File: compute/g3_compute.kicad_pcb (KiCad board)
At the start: 4 copper layers, 100 x 100 mm, 106 parts, among them IC101 CD74AC153M96, J101 Conn_01x09_Male, J102 53398-0871, J103 Temp_Connector_1x4, J104 53398-0671, J105 Conn_01x10_Male, J106 Pi_Connector, J107 Conn_01x06_Male, J108 CONSMA001-SMD-G, J109 CONSMA001-SMD-G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

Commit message: First alternative revision
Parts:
- added G***: LOGO, Perch:perch_logo, F.Cu at (116.4, 132.3)
- moved C217 119.4 mm to (111.7, 119.8), turned to 270 degrees
- moved C216 112.0 mm to (115.1, 119.8), turned to 270 degrees
- moved C214 109.1 mm to (119.8, 116.7), turned to 90 degrees
- moved L207 108.0 mm to (113.4, 119.2), turned to 180 degrees
- moved C215 102.6 mm to (118.0, 119.3), turned to 180 degrees
- moved C213 101.6 mm to (123.0, 120.5), turned to 270 degrees
- moved C212 100.8 mm to (127.2, 119.9), turned to 180 degrees
- moved U202 98.0 mm to (120.8, 119.3), turned to 180 degrees
- moved C207 98.0 mm to (132.3, 120.5), turned to 270 degrees
- moved L206 95.8 mm to (124.8, 119.9), turned to 180 degrees
- moved L205 95.3 mm to (130.6, 119.9), turned to 180 degrees
- moved C209 94.2 mm to (130.6, 121.0), turned to 180 degrees
- moved C205 93.4 mm to (134.5, 121.6), turned to 270 degrees
- moved R201 93.3 mm to (118.7, 116.7), turned to 90 degrees
- moved C211 92.7 mm to (128.8, 120.5), turned to 270 degrees
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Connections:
- C208 pad 1: Net-(C206-Pad1) -> Net-(C208-Pad1)
- C215 pad 1: /LoRa Module/ANT -> Net-(C215-Pad1)
- IC101 pad 10: /GPS_TX -> /GPS_RX
- IC101 pad 11: /E5_TX -> /E5_RX
- IC101 pad 12: /LOAD_TX -> /LOAD_RX
- IC101 pad 13: /CPPC_TX -> /CPPC_RX
- IC101 pad 14: /MUX_SELB -> /MUX_SELA
- IC101 pad 2: /MUX_SELA -> /MUX_SELB
- IC101 pad 3: /CPPC_RX -> /CPPC_TX
- IC101 pad 4: /LOAD_RX -> /LOAD_TX
- IC101 pad 5: /E5_RX -> /E5_TX
- IC101 pad 6: /GPS_RX -> /GPS_TX
- IC101 pad 7: /PI_TXD0 -> /PI_RXD0
- IC101 pad 9: /PI_RXD0 -> /PI_TXD0
- J105 pad 10: /PI_GPIO26 -> /PI_GPIO5
- J105 pad 4: /PI_GPIO25 -> /PI_GPIO27
- J105 pad 6: /PI_GPIO8 -> /PI_GPIO4
- J105 pad 9: /PI_GPIO19 -> /PI_GPIO6
- J106 pad 12: /~PS_CC_QON -> /PS_BOOST_PS
- J106 pad 13: /PS_BOOST_PS -> /PI_GPIO27
- J106 pad 22: /PI_GPIO25 -> /~PS_CC_QON
- J106 pad 24: /PI_GPIO8 -> /CPPC_INT
- J106 pad 26: /GPS_3DFIX -> /MUX_SELA
- J106 pad 29: /~GPS_RESET -> /PI_GPIO5
- J106 pad 31: /GPS_SW_EN -> /PI_GPIO6
- J106 pad 32: /CPPC_INT -> /MUX_SELB
- J106 pad 35: /PI_GPIO19 -> /GPS_SW_EN
- J106 pad 37: /PI_GPIO26 -> /~GPS_RESET
- J106 pad 38: /MUX_SELA -> /~E5_BOOT
- J106 pad 40: /MUX_SELB -> /GPS_3DFIX
- J106 pad 7: /~E5_BOOT -> /PI_GPIO4
- L203 pad 1: Net-(L203-Pad1) -> Net-(C208-Pad1)
- R108 pad 2: /MUX_SELA -> /MUX_SELB
- R109 pad 2: /MUX_SELB -> /MUX_SELA
- TP124 pad 1: /PI_GPIO8 -> /PI_GPIO4
- TP130 pad 1: /PI_GPIO19 -> /PI_GPIO6
- TP134 pad 1: /PI_GPIO25 -> /PI_GPIO27
- TP135 pad 1: /PI_GPIO26 -> /PI_GPIO5
- U201 pad 22: Net-(L203-Pad1) -> Net-(C208-Pad1)
- U202 pad 5: /LoRa Module/ANT -> Net-(C215-Pad1)
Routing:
- net /GPS_3DFIX: track 134.1 -> 19.9 mm, vias 2 -> 0
- net /ANT: track 116.6 -> 4.83 mm, vias 2 -> 0
- net /~GPS_RESET: track 118.2 -> 32.1 mm, vias 2 -> 0
- net +5V: track 100.6 -> 16.1 mm
- net /LOAD_RX: track 76.7 -> 8.50 mm
- net /PI_TXD0: track 79.6 -> 13.1 mm, vias 2 -> 0
- net /PI_GPIO25: track 60.5 -> 0.00 mm
- net /PI_GPIO8: track 59.5 -> 0.00 mm
- net /GPS_SW_EN: track 80.2 -> 23.3 mm, vias 2 -> 0
- net /PI_GPIO19: track 56.3 -> 0.00 mm
- net /PI_GPIO13: track 56.3 -> 0.00 mm
- net /PI_GPIO26: track 56.3 -> 0.00 mm
- net /PI_GPIO10: track 55.4 -> 0.00 mm
- net /PI_GPIO9: track 54.9 -> 0.00 mm
- net /PI_GPIO22: track 54.6 -> 0.00 mm
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- added copper zone on F.Cu, net +3V3
- added copper zone on 3V3, net +5V
- added copper zone on F.Cu, net +5V
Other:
- outline, holes or cut-outs redrawn
- board text added: "GPIO17"

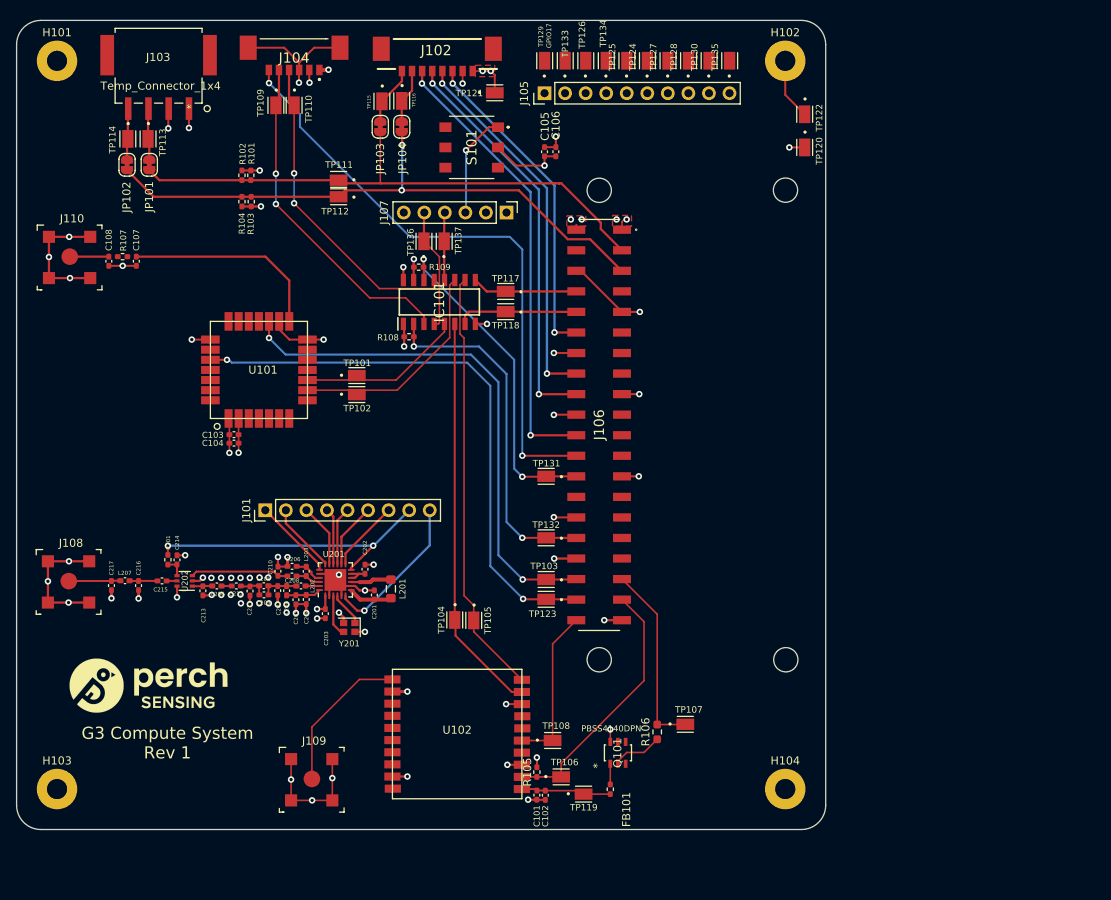
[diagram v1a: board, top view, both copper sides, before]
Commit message: Finishing GPIO header wiring
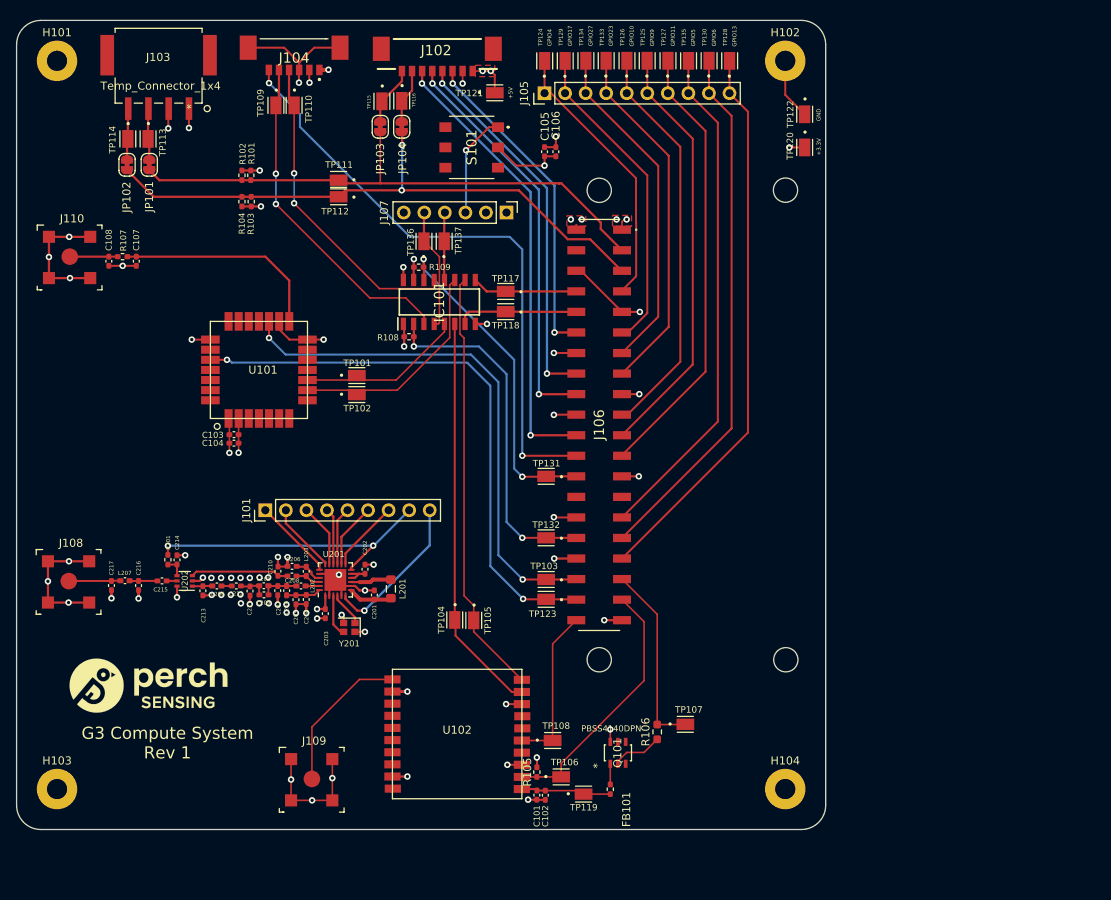
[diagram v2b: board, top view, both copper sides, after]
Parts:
- moved TP124 12.7 mm to (165.3, 55.0)
- moved TP126 5.09 mm to (175.4, 55.0)
- moved TP128 5.08 mm to (188.1, 55.0)
- moved TP135 5.08 mm to (183.1, 55.0)
- moved TP133 5.06 mm to (172.9, 55.0)
- moved TP129 2.54 mm to (167.8, 55.0)
- moved TP134 2.52 mm to (170.4, 55.0)
- moved TP125 2.51 mm to (177.9, 55.0)
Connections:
- J105 pad 1: /PI_GPIO17 -> /PI_GPIO4
- J105 pad 10: /PI_GPIO5 -> /PI_GPIO13
- J105 pad 2: /PI_GPIO22 -> /PI_GPIO17
- J105 pad 3: /PI_GPIO10 -> /PI_GPIO27
- J105 pad 4: /PI_GPIO27 -> /PI_GPIO22
- J105 pad 5: /PI_GPIO9 -> /PI_GPIO10
- J105 pad 6: /PI_GPIO4 -> /PI_GPIO9
- J105 pad 8: /PI_GPIO13 -> /PI_GPIO5
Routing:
- net /PI_GPIO13: track 0.00 -> 68.9 mm
- net /PI_GPIO6: track 0.00 -> 65.8 mm
- net /PI_GPIO5: track 0.00 -> 62.8 mm
- net /PI_GPIO11: track 0.00 -> 55.0 mm
- net /PI_GPIO9: track 0.00 -> 52.2 mm
- net /PI_GPIO10: track 0.00 -> 49.9 mm
- net /PI_GPIO22: track 0.00 -> 44.3 mm
- net /PI_GPIO27: track 0.00 -> 41.7 mm
- net /PI_GPIO17: track 0.00 -> 39.5 mm
- net /PI_GPIO4: track 0.00 -> 34.4 mm
- net /E5_RFIO: track 25.2 -> 26.3 mm
- net /ANT: track 4.83 -> 5.92 mm
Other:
- board text added: "+3.3V"
- board text added: "+5V"
- board text added: "GND"
- board text added: "GPIO10"
- board text added: "GPIO11"
- board text added: "GPIO13"
- board text added: "GPIO23"
- board text added: "GPIO27"
- board text added: "GPIO4"
- board text added: "GPIO5"
- board text added: "GPIO6"
- board text added: "GPIO9"

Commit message: Adding more testpoints, without breaking things
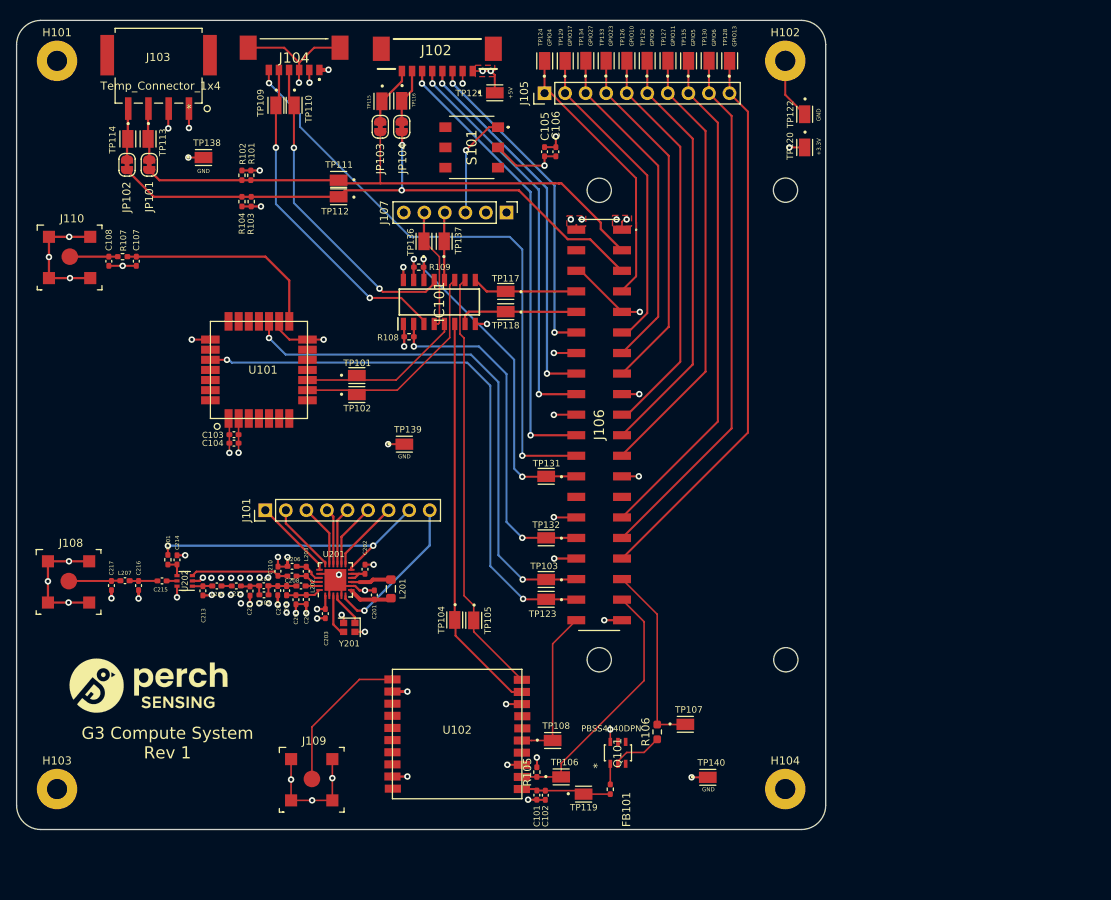
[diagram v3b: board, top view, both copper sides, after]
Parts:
- added TP138: TestPoint, Perch:HARWIN_S2751-46R, F.Cu at (123.1, 67.0)
- added TP139: TestPoint, Perch:HARWIN_S2751-46R, F.Cu at (147.9, 102.4)
- added TP140: TestPoint, Perch:HARWIN_S2751-46R, F.Cu at (185.4, 143.6)
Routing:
- net GND: track 178.4 -> 184.3 mm, vias 64 -> 67

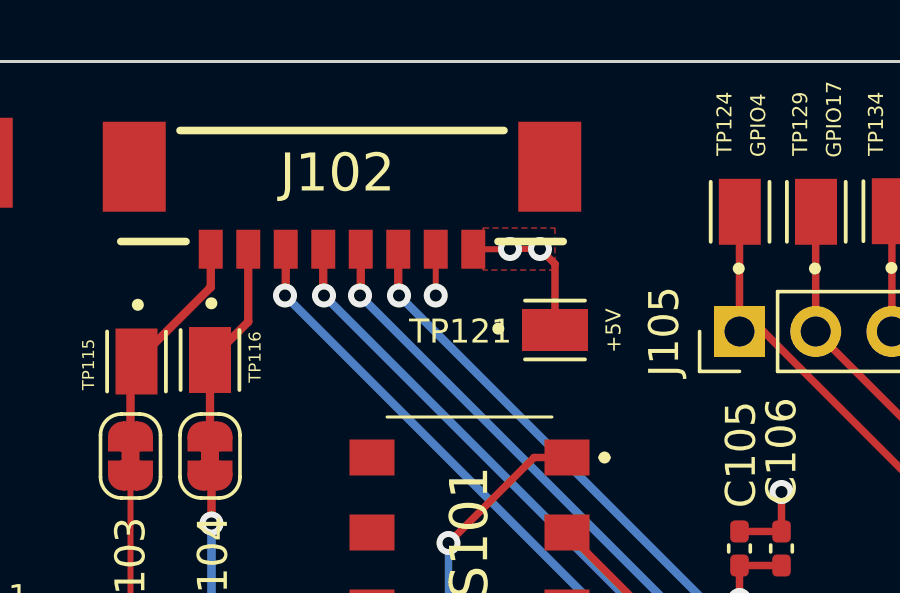
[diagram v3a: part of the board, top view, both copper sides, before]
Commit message: Matching GND paths from Power Subsystem
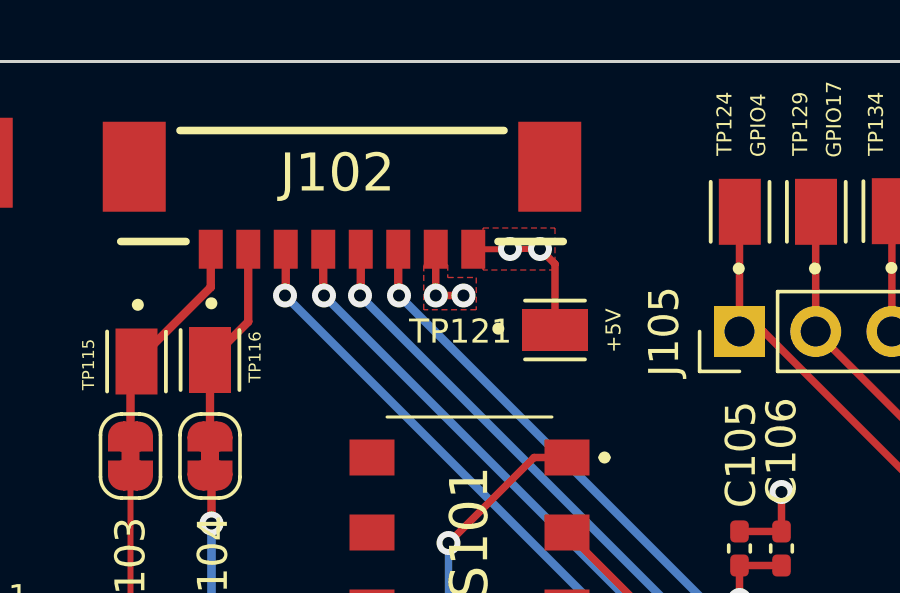
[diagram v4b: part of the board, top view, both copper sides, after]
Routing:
- net GND: track 184.3 -> 185.1 mm, vias 67 -> 68
- added copper zone on F.Cu, net GND

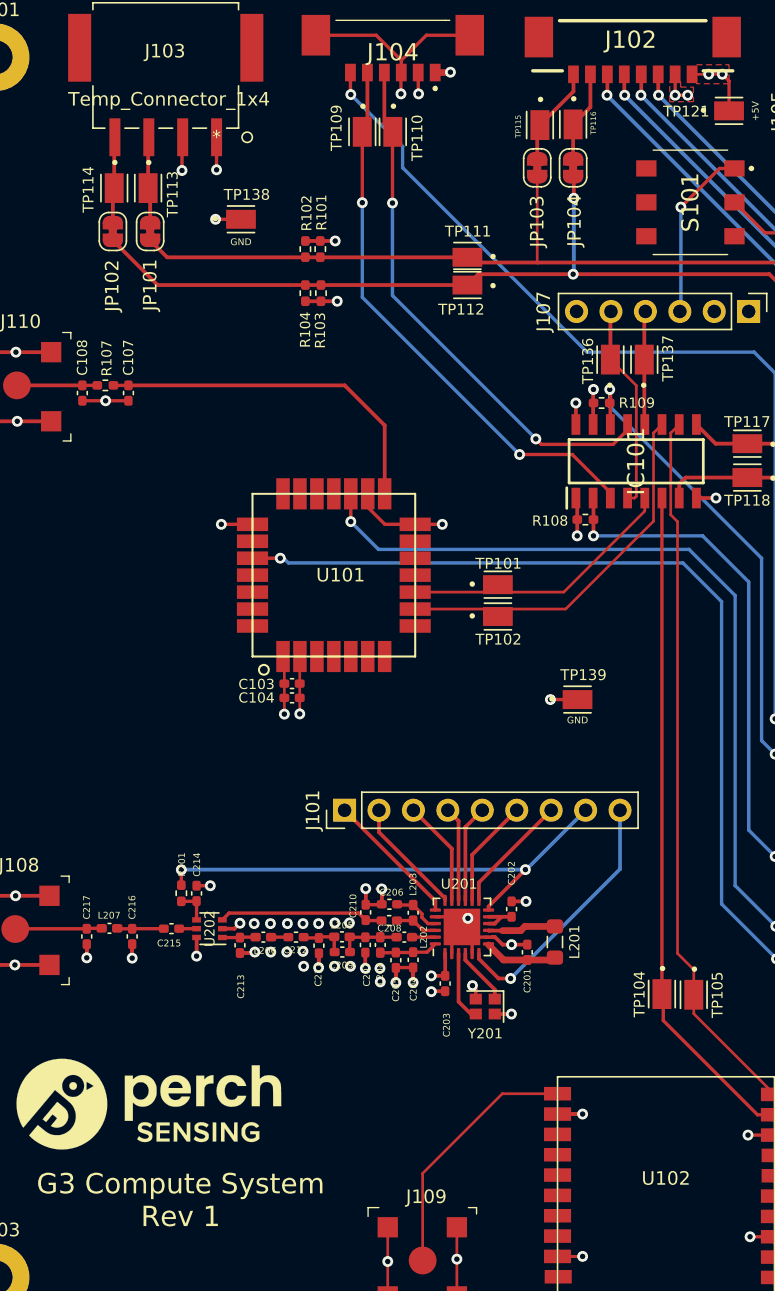
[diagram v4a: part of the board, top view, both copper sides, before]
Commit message: Adding waveguides and note to compute RF signals
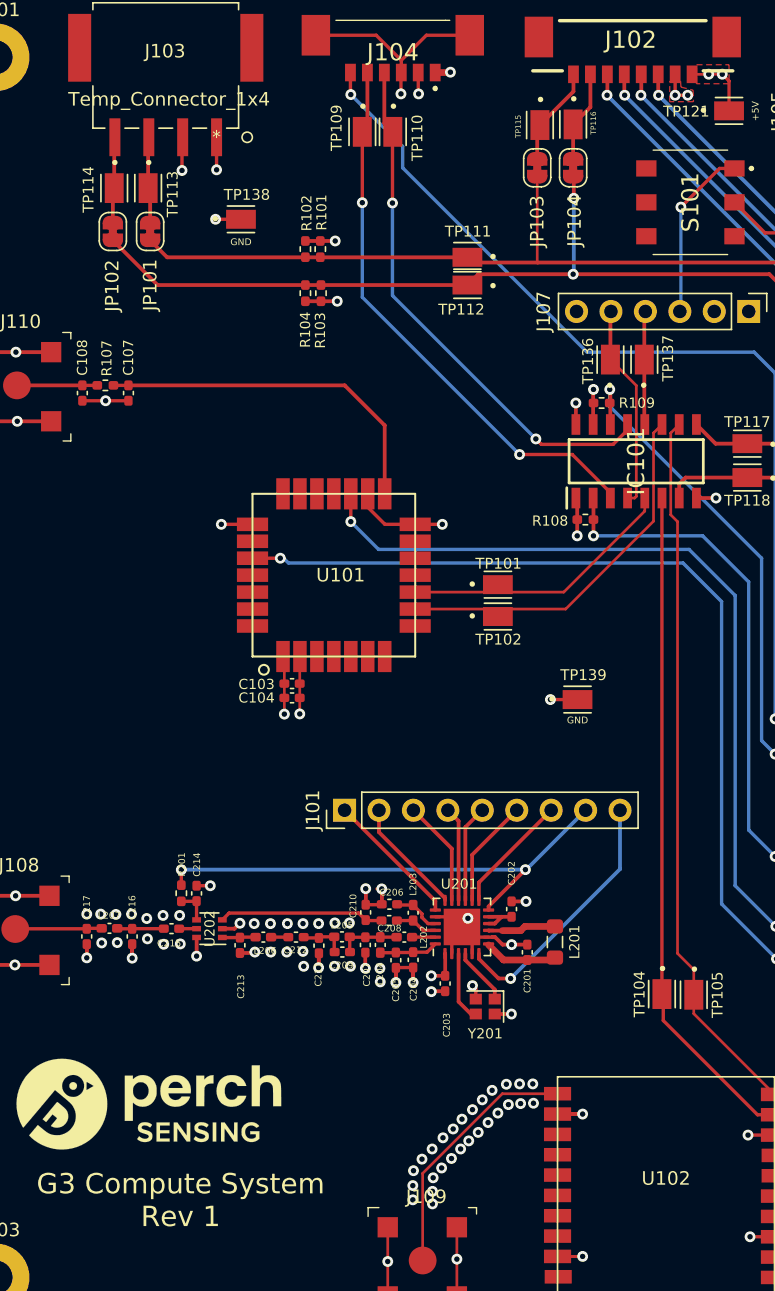
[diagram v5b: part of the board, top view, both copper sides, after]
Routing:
- net GND: vias 68 -> 107
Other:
- board text added: "NOTE: Should we be using this technique for RF signals? Seen in LoRa example shield for high frequency signals"

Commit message: Making suggested changes
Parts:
- moved TP120 5.38 mm to (193.2, 62.4), turned to 180 degrees
- moved TP122 0.81 mm to (197.2, 62.4), turned to 180 degrees
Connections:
- H101 pad 1: GND -> Earth
- H102 pad 1: GND -> Earth
- H103 pad 1: GND -> Earth
- H104 pad 1: GND -> Earth
- IC101 pad 10: /GPS_RX -> /LOAD_RX
- IC101 pad 11: /E5_RX -> /GPS_RX
- IC101 pad 12: /LOAD_RX -> /E5_RX
- IC101 pad 4: /LOAD_TX -> /E5_TX
- IC101 pad 5: /E5_TX -> /GPS_TX
- IC101 pad 6: /GPS_TX -> /LOAD_TX
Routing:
- net GND: track 185.1 -> 179.6 mm, vias 107 -> 154
- net +3V3: track 28.8 -> 31.0 mm
- net /LOAD_TX: track 15.2 -> 16.8 mm
- net /PI_SCL: track 74.2 -> 75.7 mm
- net /LOAD_RX: track 8.50 -> 9.55 mm
- net /PI_SDA: track 69.7 -> 70.3 mm
- net /GPS_RX: track 52.8 -> 53.4 mm
- net /GPS_TX: track 49.7 -> 50.2 mm

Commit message: Changing +5v power supply from UART LOADER
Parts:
- removed G***: LOGO, Perch:perch_logo
- removed S101: 452403012014, Perch:452403012014_Switch
- added J111: Conn_01x02_Male, Connector_PinHeader_2.54mm:PinHeader_1x02_P2.54mm_Vertical_SMD_Pin1Left, F.Cu at (154.8, 65.2)
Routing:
- net +5V: track 16.1 -> 18.0 mm
- net Net-(J107-Pad3): track 12.9 -> 11.5 mm
